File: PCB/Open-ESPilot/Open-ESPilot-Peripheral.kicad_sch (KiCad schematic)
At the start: 57 parts, among them J10 UART1, J11 UART2, J12 I2C, J13 Micro SD Card Breakout, J14 LED out, J5 PWM output, J6 RC in, J7 Vx, J8 GND, J9 UART0, M2 GY91, Q2 BC847, Q3 BC847, U5 Micro_SD_Card

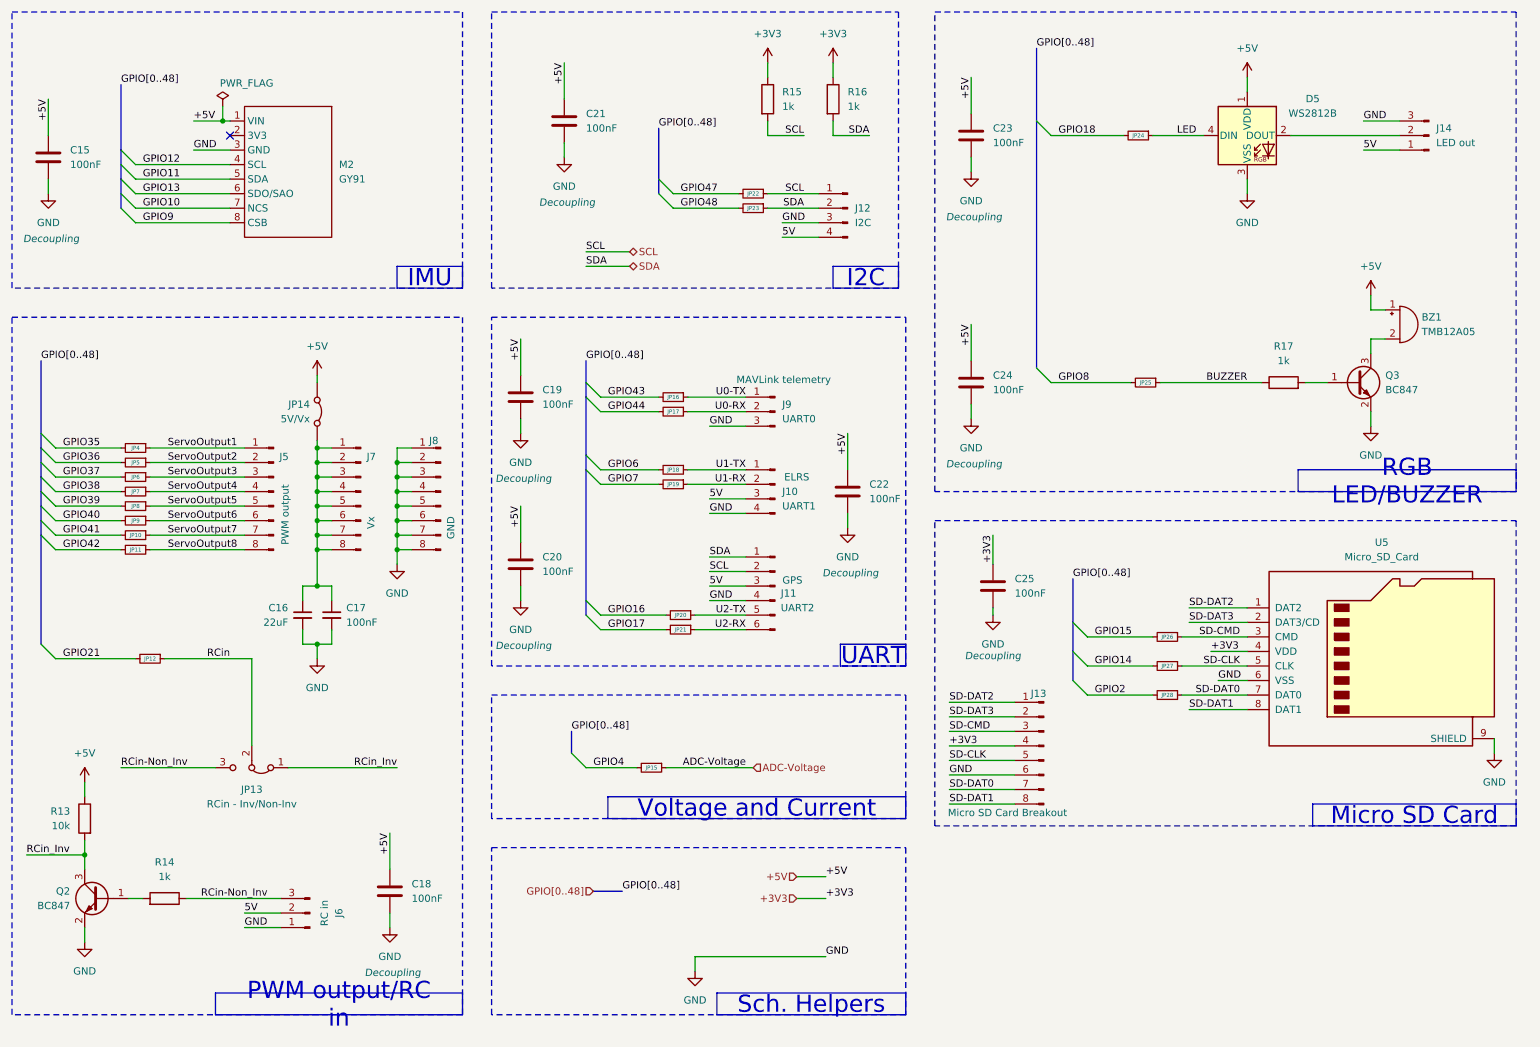
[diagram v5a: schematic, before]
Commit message: Started routing. I have few things there. Fixed schematic.
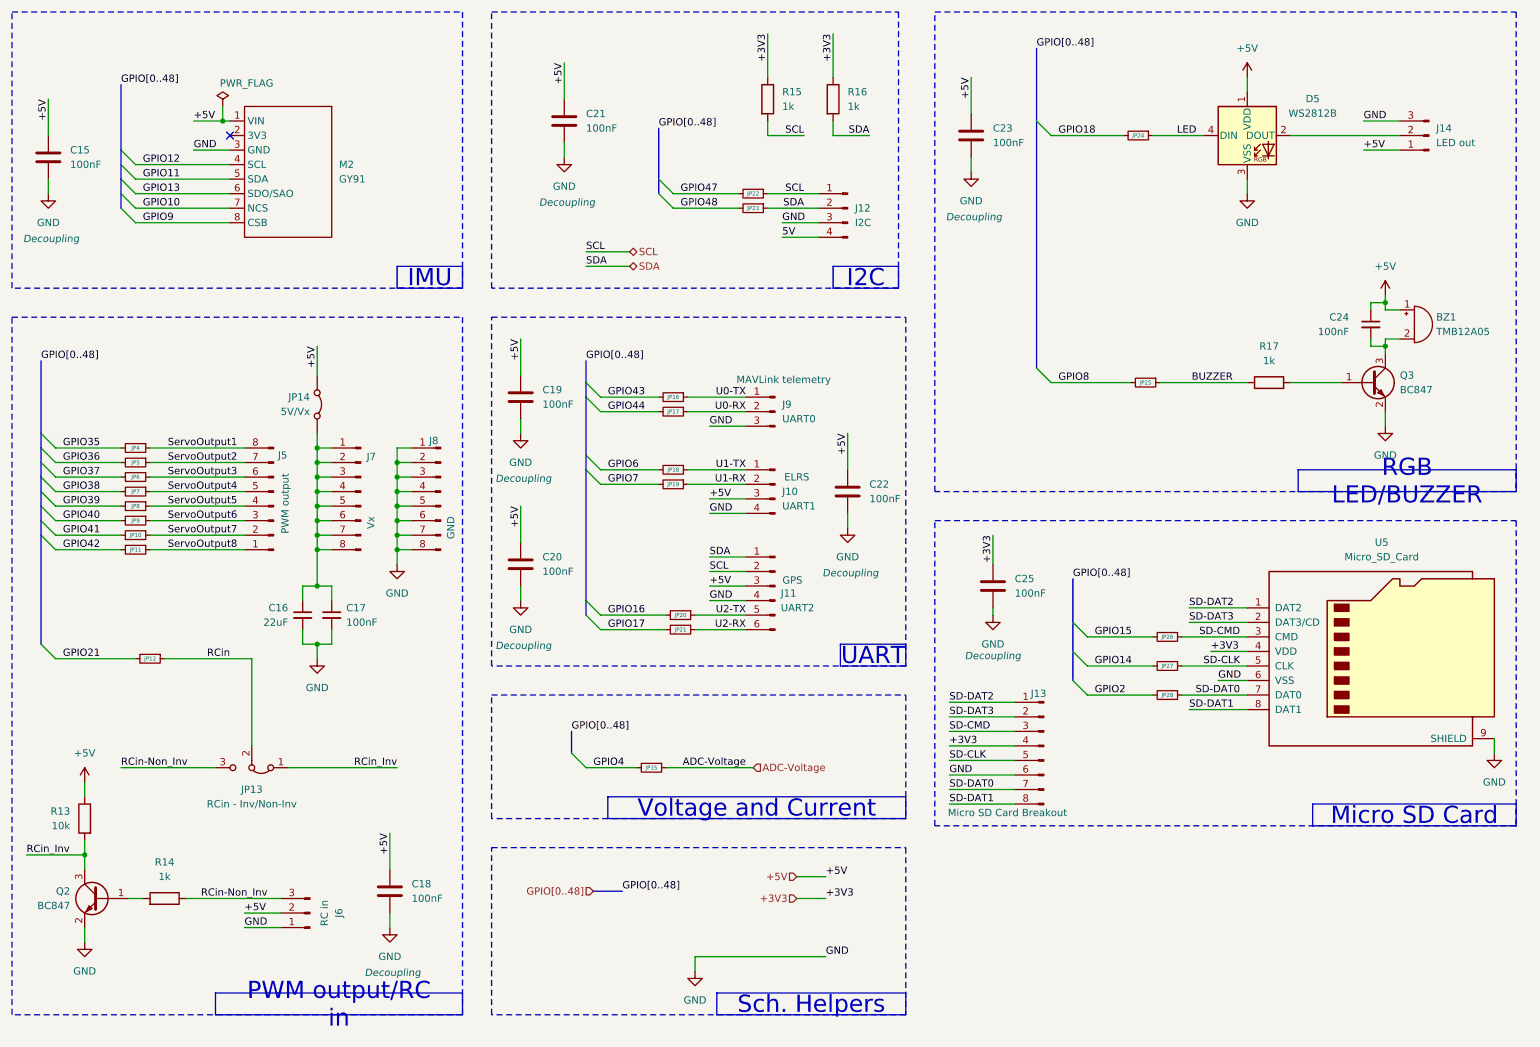
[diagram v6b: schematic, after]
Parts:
- C24: symbol Device:C -> Device:C_Small
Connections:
- net +5V: now also J10.3 (Pin_3), J11.3 (Pin_3), J14.1 (Pin_1), J6.2 (Pin_2)
- net 5V: no longer J10.3 (Pin_3), J11.3 (Pin_3), J14.1 (Pin_1), J6.2 (Pin_2)
- net GND: no longer C24.2
- net ServoOutput1: now also J5.8 (Pin_8); no longer J5.1 (Pin_1)
- net ServoOutput2: now also J5.7 (Pin_7); no longer J5.2 (Pin_2)
- net ServoOutput3: now also J5.6 (Pin_6); no longer J5.3 (Pin_3)
- net ServoOutput4: now also J5.5 (Pin_5); no longer J5.4 (Pin_4)
- net ServoOutput5: now also J5.4 (Pin_4); no longer J5.5 (Pin_5)
- net ServoOutput6: now also J5.3 (Pin_3); no longer J5.6 (Pin_6)
- net ServoOutput7: now also J5.2 (Pin_2); no longer J5.7 (Pin_7)
- net ServoOutput8: now also J5.1 (Pin_1); no longer J5.8 (Pin_8)
- net at BZ1.2 (-), Q3.3 (C): now also C24.2
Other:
- moved on the sheet: BZ1, C24, J5, JP14, Q3, R17

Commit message: halve of the PCB is routed.
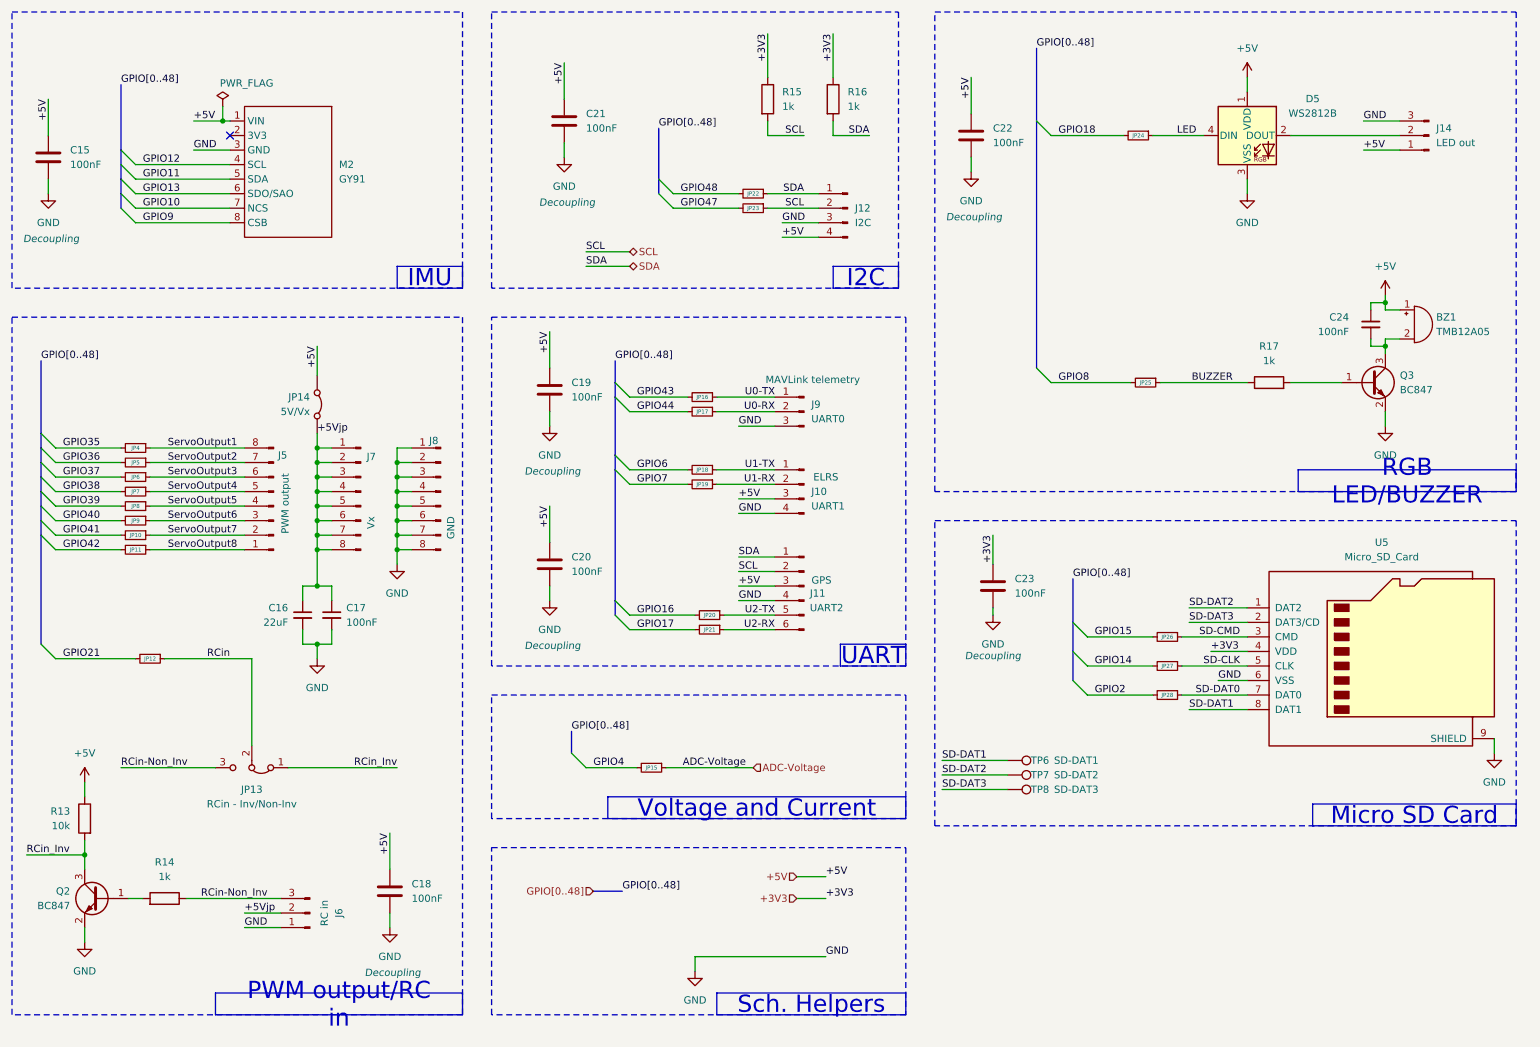
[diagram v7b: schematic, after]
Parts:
- removed C19: 100nF, Capacitor_SMD:C_0805_2012Metric_Pad1.18x1.45mm_HandSolder, symbol Device:C
- removed J13: Micro SD Card Breakout, Connector_PinHeader_2.54mm:PinHeader_1x08_P2.54mm_Vertical, symbol Connector:Conn_01x08_Pin
- added TP6: SD-DAT1, TestPoint:TestPoint_Pad_D2.0mm, symbol Connector:TestPoint
- added TP7: SD-DAT2, TestPoint:TestPoint_Pad_D2.0mm, symbol Connector:TestPoint
- added TP8: SD-DAT3, TestPoint:TestPoint_Pad_D2.0mm, symbol Connector:TestPoint
- M2: footprint GY-90:GY-90 -> GY-91:GY-91
- renumbered C22 to C19, C23 to C22, C25 to C23, JP23 to JP22, JP22 to JP23
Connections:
- net 5V is gone; now on net +5V: J12.4 (Pin_4)
- net +5V: no longer J6.2 (Pin_2)
- net SCL: now also J12.2 (Pin_2); no longer J12.1 (Pin_1)
- net SD-DAT1: now also TP6.1
- net SD-DAT2: now also TP7.1
- net SD-DAT3: now also TP8.1
- net SDA: now also J12.1 (Pin_1); no longer J12.2 (Pin_2)
- net +5Vjp: now reaches C16.1, C17.1, J7.1 (Pin_1), J7.2 (Pin_2), J7.3 (Pin_3), J7.4 (Pin_4), J7.5 (Pin_5), J7.6 (Pin_6), J7.7 (Pin_7), J7.8 (Pin_8), JP14.1 (A)
- net +5Vjp: now also J6.2 (Pin_2)
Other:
- moved on the sheet: C19, C20, J10, J11, J9, JP16, JP17, JP18, JP19, JP20, JP21, JP22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

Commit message: I'm rushing it! :( Finished the PCB
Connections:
- net +5V: now also J6.2 (Pin_2)
- net +5Vjp: no longer J6.2 (Pin_2)
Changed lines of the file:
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@@
 	(wire
 		(pts
+			(xy 29.21 148.59) (xy 29.21 154.94)
+		)
+		(stroke
+			(width 0)
+			(type default)
+		)
+	)
+	(wire
+		(pts
 			(xy 254 74.93) (xy 254 76.2)
 		)
@@
 		)
 	)
-	(wire
-		(pts
-			(xy 29.21 152.4) (xy 29.21 154.94)
-		)
-		(stroke
-			(width 0)
-			(type default)
-		)
-	)
 	(bus
 		(pts
@@
 		)
 	)
-	(label "+5Vjp"
+	(label "+5V"
 		(at 57.15 175.26 0)
 		(effects
@@
 		)
 	)
+	(label "+5V"
+		(at 29.21 148.59 270)
+		(effects
+			(font
+				(size 1.27 1.27)
+			)
+			(justify right bottom)
+		)
+	)
 	(label "BUZZER"
 		(at 229.87 82.55 180)
@@
 					(unit 1)
 				)
-			)
-		)
-	)
-	(symbol
-		(lib_id "power:+5V")
-		(at 29.21 152.4 0)
-		(mirror y)
-		(unit 1)
-		(exclude_from_sim no)
-		(in_bom yes)
-		(on_board yes)
-		(dnp no)
-		(property "Reference" "#PWR041"
-			(at 29.21 156.21 0)
-			(effects
-				(font
-					(size 1.27 1.27)
-				)
-				(hide yes)
-			)
-		)
-		(property "Value" "+5V"
-			(at 29.21 147.32 0)
-			(effects
-				(font
-					(size 1.27 1.27)
-				)
-			)
-		)
-		(property "Footprint" ""
-			(at 29.21 152.4 0)
-			(effects
-				(font
-					(size 1.27 1.27)
-				)
-				(hide yes)
-			)
-		)
-		(property "Datasheet" ""
-			(at 29.21 152.4 0)
-			(effects
-				(font
-					(size 1.27 1.27)
-				)
-				(hide yes)
-			)
-		)
-		(property "Description" "Power symbol creates a global label with name \"+5V\""
-			(at 29.21 152.4 0)
-			(effects
-				(font
-					(size 1.27 1.27)
-				)
-				(hide yes)
-			)
-		)
-		(pin "1"
-		)
-		(instances
-			(project "Open-ESPilot"
-				(path "/2992e60d-a645-4cd7-90ae-fe72311b6bee/e6a81ea1-6816-412d-a6dc-b491c7035238"
-					(reference "#PWR041")
-					(unit 1)
-				)
